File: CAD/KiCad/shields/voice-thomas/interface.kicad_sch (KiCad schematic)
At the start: 2 parts

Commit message: Route the shield set and validate shared interfaces
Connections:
- net +5V: no longer names the net of JV1.5
- no-connect marks 0 -> 1
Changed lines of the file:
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@@
 (kicad_sch (version 20250114) (generator "eeschema") (generator_version "9.0")
  (paper "A3")
-          (title_block (title "voice-thomas / interface") (date "2026-10-01") (rev "A-review")
+          (title_block (title "voice-thomas / interface") (date "2026-10-04") (rev "A-prototype")
             (company "Colloquy of Mobiles") (comment 1 "Prototype: verify harness polarity and sensor values before connection"))
           (text "COLLOQUY / VOICE-THOMAS / INTERFACE" (at 15.24 15.24 0) (effects (font (size 2.032 2.032) (bold yes)) (justify left top)))
@@
 (wire (pts (xy 81.2800 71.1200) (xy 78.7400 71.1200)) (stroke (width 0) (type default)))
 (global_label "AGND" (shape bidirectional) (at 78.7400 71.1200 180) (effects (font (size 0.95 0.95)) (justify right)) (property "Intersheetrefs" "${INTERSHEET_REFS}" (at 78.7400 71.1200 0) (effects (font (size 1.016 1.016))  (hide yes))))
-(wire (pts (xy 81.2800 76.2000) (xy 78.7400 76.2000)) (stroke (width 0) (type default)))
-(global_label "+5V" (shape bidirectional) (at 78.7400 76.2000 180) (effects (font (size 0.95 0.95)) (justify right)) (property "Intersheetrefs" "${INTERSHEET_REFS}" (at 78.7400 76.2000 0) (effects (font (size 1.016 1.016))  (hide yes))))
+(no_connect (at 81.2800 76.2000))
 (wire (pts (xy 81.2800 81.2800) (xy 78.7400 81.2800)) (stroke (width 0) (type default)))
 (global_label "AGND" (shape bidirectional) (at 78.7400 81.2800 180) (effects (font (size 0.95 0.95)) (justify right)) (property "Intersheetrefs" "${INTERSHEET_REFS}" (at 78.7400 81.2800 0) (effects (font (size 1.016 1.016))  (hide yes))))

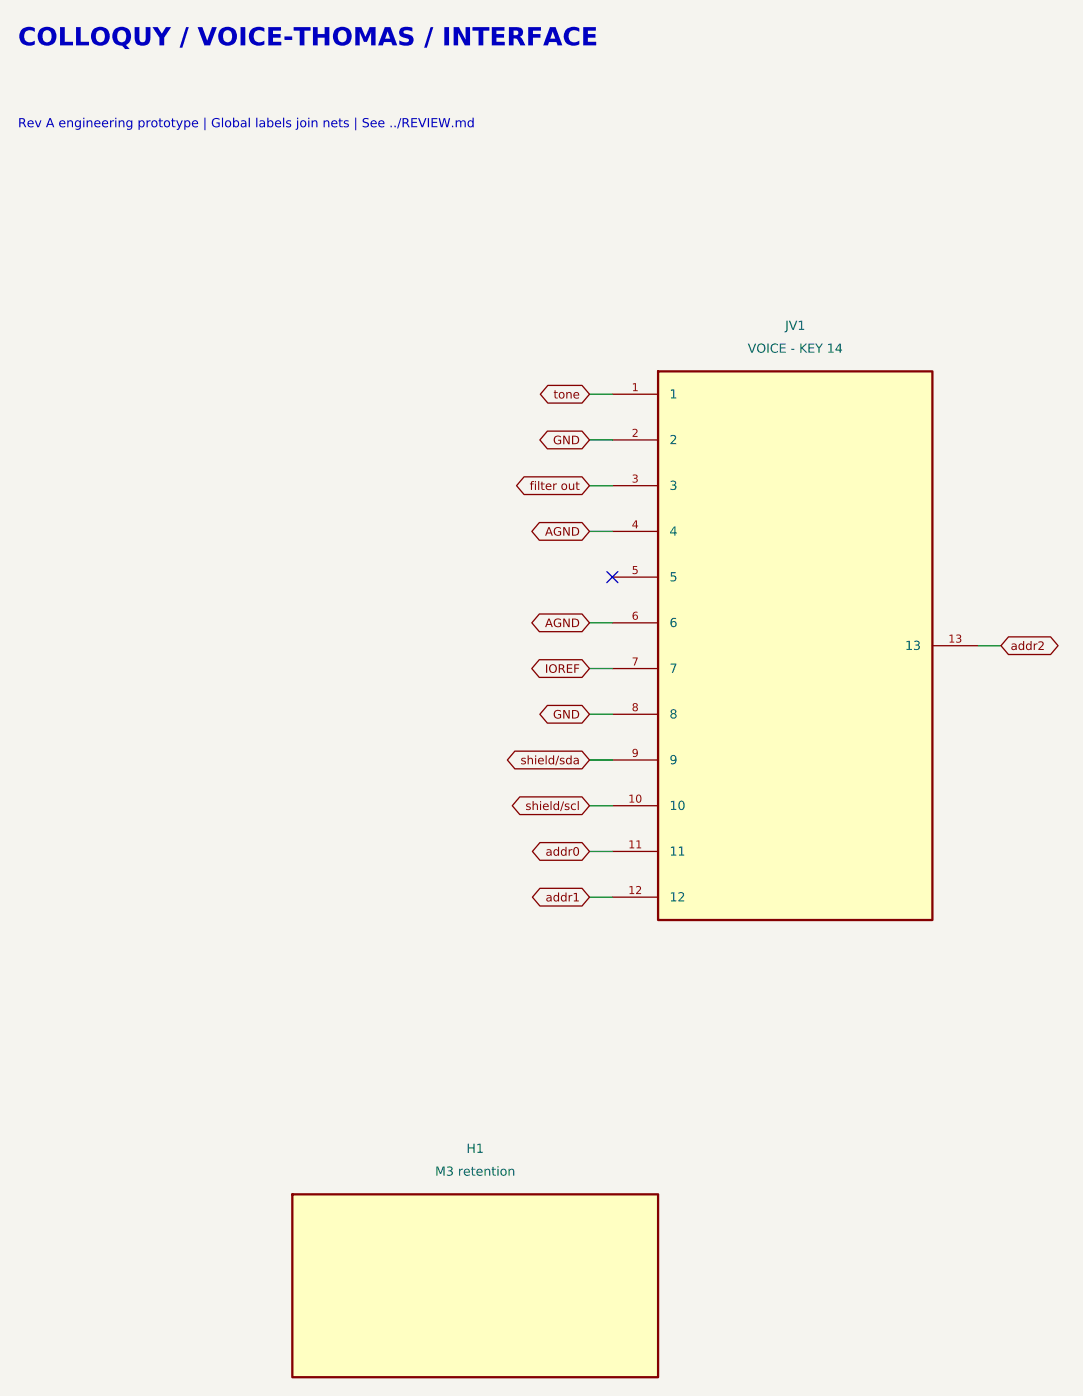
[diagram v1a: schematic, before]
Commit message: Remove shield identification and adopt the simplified connector and Teensy pin maps
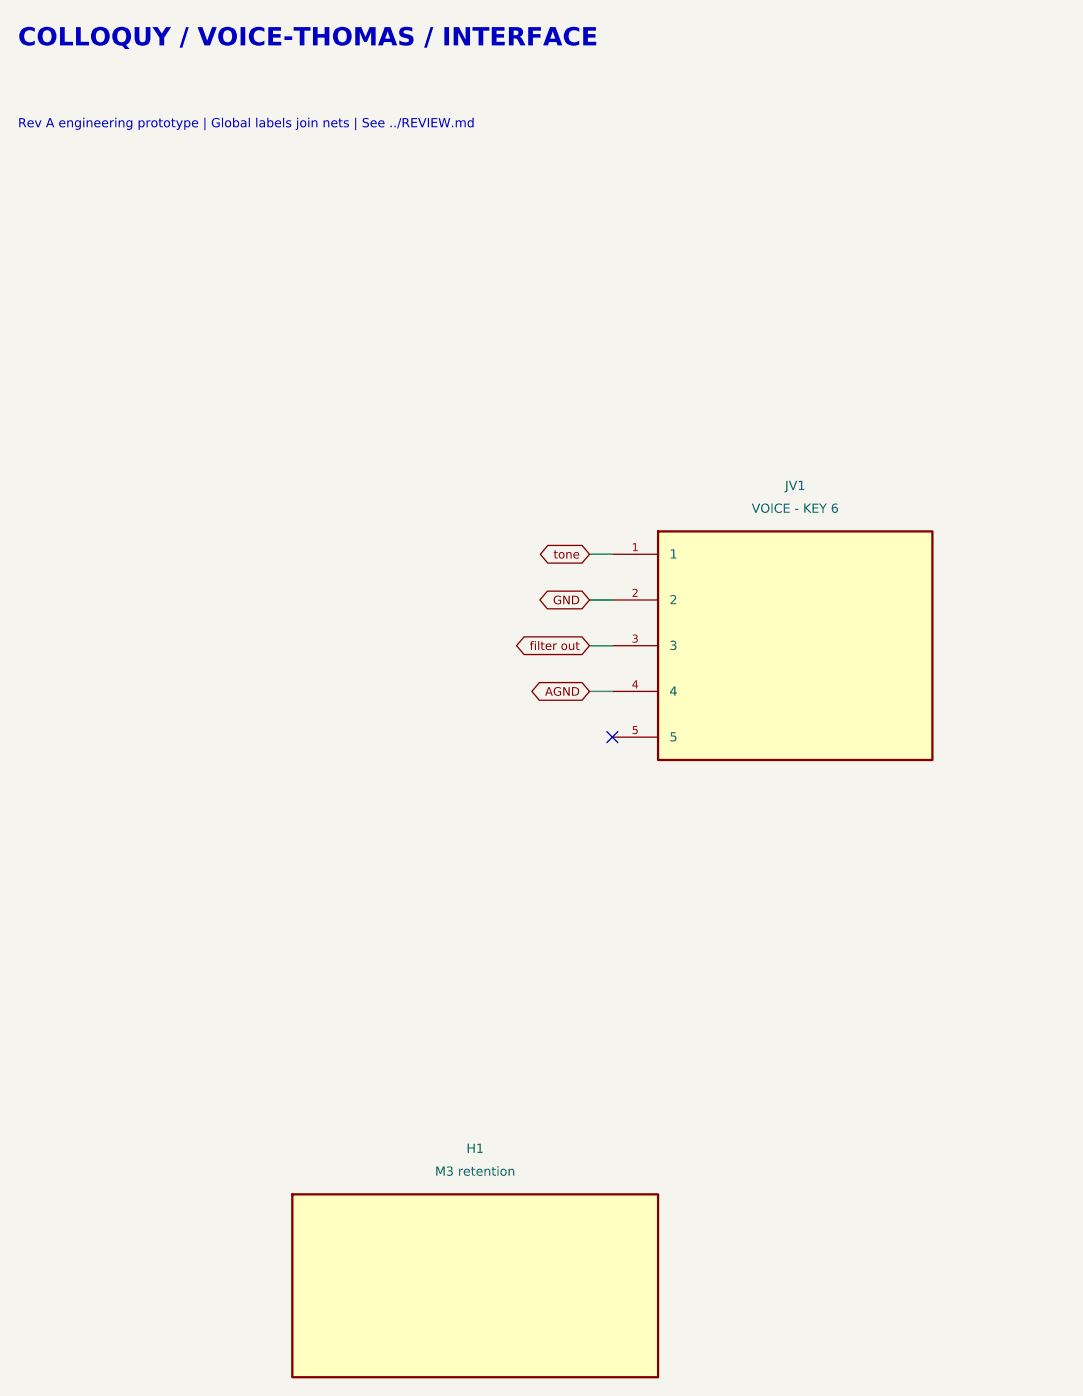
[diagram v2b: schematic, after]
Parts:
- JV1: value VOICE - KEY 14 -> VOICE - KEY 6; footprint Shields:Socket_2x07_Key14 -> Shields:Socket_2x03_Key6
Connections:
- net AGND: no longer JV1.6
- net GND: no longer JV1.8
- removed net IOREF: JV1.7
- removed net addr0: JV1.11
- removed net addr1: JV1.12
- removed net addr2: JV1.13
- removed net shield/scl: JV1.10
- removed net shield/sda: JV1.9
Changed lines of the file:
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@@
 (text "Rev A engineering prototype | Global labels join nets | See ../REVIEW.md" (at 15.24 25.4 0) (effects (font (size 1.016 1.016) ) (justify left top)))
 (symbol (lib_id "Colloquy:JV1") (at 101.6000 83.8200 0) (unit 1) (exclude_from_sim no) (in_bom yes) (on_board yes) (dnp no)
-(property "Reference" "JV1" (at 101.6000 48.2600 0) (effects (font (size 1.016 1.016))  ))
-(property "Value" "VOICE - KEY 14" (at 101.6000 50.8000 0) (effects (font (size 1.016 1.016))  ))
-(property "Footprint" "Shields:Socket_2x07_Key14" (at 101.6000 83.8200 0) (effects (font (size 1.27 1.27))  (hide yes)))
+(property "Reference" "JV1" (at 101.6000 66.0400 0) (effects (font (size 1.016 1.016))  ))
+(property "Value" "VOICE - KEY 6" (at 101.6000 68.5800 0) (effects (font (size 1.016 1.016))  ))
+(property "Footprint" "Shields:Socket_2x03_Key6" (at 101.6000 83.8200 0) (effects (font (size 1.27 1.27))  (hide yes)))
 (property "Datasheet" "" (at 101.6000 83.8200 0) (effects (font (size 1.27 1.27))  (hide yes)))
 (property "Description" "" (at 101.6000 83.8200 0) (effects (font (size 1.27 1.27))  (hide yes)))
@@
 (pin "4")
 (pin "5")
-(pin "6")
-(pin "7")
-(pin "8")
-(pin "9")
-(pin "10")
-(pin "11")
-(pin "12")
-(pin "13")
 (instances (project "voice-thomas" (path "/b263c855-4a4b-5b9c-a9f0-0ad21dbcdee8/3b9bbe2e-8467-5b31-a4a8-4ed75210e53f" (reference "JV1") (unit 1)))))
-(wire (pts (xy 81.2800 55.8800) (xy 78.7400 55.8800)) (stroke (width 0) (type default)))
-(global_label "tone" (shape bidirectional) (at 78.7400 55.8800 180) (effects (font (size 0.95 0.95)) (justify right)) (property "Intersheetrefs" "${INTERSHEET_REFS}" (at 78.7400 55.8800 0) (effects (font (size 1.016 1.016))  (hide yes))))
-(wire (pts (xy 81.2800 60.9600) (xy 78.7400 60.9600)) (stroke (width 0) (type default)))
-(global_label "GND" (shape bidirectional) (at 78.7400 60.9600 180) (effects (font (size 0.95 0.95)) (justify right)) (property "Intersheetrefs" "${INTERSHEET_REFS}" (at 78.7400 60.9600 0) (effects (font (size 1.016 1.016))  (hide yes))))
-(wire (pts (xy 81.2800 66.0400) (xy 78.7400 66.0400)) (stroke (width 0) (type default)))
-(global_label "filter out" (shape bidirectional) (at 78.7400 66.0400 180) (effects (font (size 0.95 0.95)) (justify right)) (property "Intersheetrefs" "${INTERSHEET_REFS}" (at 78.7400 66.0400 0) (effects (font (size 1.016 1.016))  (hide yes))))
-(wire (pts (xy 81.2800 71.1200) (xy 78.7400 71.1200)) (stroke (width 0) (type default)))
-(global_label "AGND" (shape bidirectional) (at 78.7400 71.1200 180) (effects (font (size 0.95 0.95)) (justify right)) (property "Intersheetrefs" "${INTERSHEET_REFS}" (at 78.7400 71.1200 0) (effects (font (size 1.016 1.016))  (hide yes))))
-(no_connect (at 81.2800 76.2000))
-(wire (pts (xy 81.2800 81.2800) (xy 78.7400 81.2800)) (stroke (width 0) (type default)))
-(global_label "AGND" (shape bidirectional) (at 78.7400 81.2800 180) (effects (font (size 0.95 0.95)) (justify right)) (property "Intersheetrefs" "${INTERSHEET_REFS}" (at 78.7400 81.2800 0) (effects (font (size 1.016 1.016))  (hide yes))))
-(wire (pts (xy 81.2800 86.3600) (xy 78.7400 86.3600)) (stroke (width 0) (type default)))
-(global_label "IOREF" (shape bidirectional) (at 78.7400 86.3600 180) (effects (font (size 0.95 0.95)) (justify right)) (property "Intersheetrefs" "${INTERSHEET_REFS}" (at 78.7400 86.3600 0) (effects (font (size 1.016 1.016))  (hide yes))))
-(wire (pts (xy 81.2800 91.4400) (xy 78.7400 91.4400)) (stroke (width 0) (type default)))
-(global_label "GND" (shape bidirectional) (at 78.7400 91.4400 180) (effects (font (size 0.95 0.95)) (justify right)) (property "Intersheetrefs" "${INTERSHEET_REFS}" (at 78.7400 91.4400 0) (effects (font (size 1.016 1.016))  (hide yes))))
-(wire (pts (xy 81.2800 96.5200) (xy 78.7400 96.5200)) (stroke (width 0) (type default)))
-(global_label "shield/sda" (shape bidirectional) (at 78.7400 96.5200 180) (effects (font (size 0.95 0.95)) (justify right)) (property "Intersheetrefs" "${INTERSHEET_REFS}" (at 78.7400 96.5200 0) (effects (font (size 1.016 1.016))  (hide yes))))
-(wire (pts (xy 81.2800 101.6000) (xy 78.7400 101.6000)) (stroke (width 0) (type default)))
-(global_label "shield/scl" (shape bidirectional) (at 78.7400 101.6000 180) (effects (font (size 0.95 0.95)) (justify right)) (property "Intersheetrefs" "${INTERSHEET_REFS}" (at 78.7400 101.6000 0) (effects (font (size 1.016 1.016))  (hide yes))))
-(wire (pts (xy 81.2800 106.6800) (xy 78.7400 106.6800)) (stroke (width 0) (type default)))
-(global_label "addr0" (shape bidirectional) (at 78.7400 106.6800 180) (effects (font (size 0.95 0.95)) (justify right)) (property "Intersheetrefs" "${INTERSHEET_REFS}" (at 78.7400 106.6800 0) (effects (font (size 1.016 1.016))  (hide yes))))
-(wire (pts (xy 81.2800 111.7600) (xy 78.7400 111.7600)) (stroke (width 0) (type default)))
-(global_label "addr1" (shape bidirectional) (at 78.7400 111.7600 180) (effects (font (size 0.95 0.95)) (justify right)) (property "Intersheetrefs" "${INTERSHEET_REFS}" (at 78.7400 111.7600 0) (effects (font (size 1.016 1.016))  (hide yes))))
-(wire (pts (xy 121.9200 83.8200) (xy 124.4600 83.8200)) (stroke (width 0) (type default)))
-(global_label "addr2" (shape bidirectional) (at 124.4600 83.8200 0) (effects (font (size 0.95 0.95)) (justify left)) (property "Intersheetrefs" "${INTERSHEET_REFS}" (at 124.4600 83.8200 0) (effects (font (size 1.016 1.016))  (hide yes))))
+(wire (pts (xy 81.2800 73.6600) (xy 78.7400 73.6600)) (stroke (width 0) (type default)))
+(global_label "tone" (shape bidirectional) (at 78.7400 73.6600 180) (effects (font (size 0.95 0.95)) (justify right)) (property "Intersheetrefs" "${INTERSHEET_REFS}" (at 78.7400 73.6600 0) (effects (font (size 1.016 1.016))  (hide yes))))
+(wire (pts (xy 81.2800 78.7400) (xy 78.7400 78.7400)) (stroke (width 0) (type default)))
+(global_label "GND" (shape bidirectional) (at 78.7400 78.7400 180) (effects (font (size 0.95 0.95)) (justify right)) (property "Intersheetrefs" "${INTERSHEET_REFS}" (at 78.7400 78.7400 0) (effects (font (size 1.016 1.016))  (hide yes))))
+(wire (pts (xy 81.2800 83.8200) (xy 78.7400 83.8200)) (stroke (width 0) (type default)))
+(global_label "filter out" (shape bidirectional) (at 78.7400 83.8200 180) (effects (font (size 0.95 0.95)) (justify right)) (property "Intersheetrefs" "${INTERSHEET_REFS}" (at 78.7400 83.8200 0) (effects (font (size 1.016 1.016))  (hide yes))))
+(wire (pts (xy 81.2800 88.9000) (xy 78.7400 88.9000)) (stroke (width 0) (type default)))
+(global_label "AGND" (shape bidirectional) (at 78.7400 88.9000 180) (effects (font (size 0.95 0.95)) (justify right)) (property "Intersheetrefs" "${INTERSHEET_REFS}" (at 78.7400 88.9000 0) (effects (font (size 1.016 1.016))  (hide yes))))
+(no_connect (at 81.2800 93.9800))
 (symbol (lib_id "Colloquy:H1") (at 66.0400 154.9400 0) (unit 1) (exclude_from_sim no) (in_bom no) (on_board yes) (dnp no)
 (property "Reference" "H1" (at 66.0400 139.7000 0) (effects (font (size 1.016 1.016))  ))
